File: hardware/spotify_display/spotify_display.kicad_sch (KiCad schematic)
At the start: 5 parts, among them SW1 SW_Push, SW2 SW_Push, SW3 SW_Push, U1 WEMOS_C3_mini, U2 ST7735

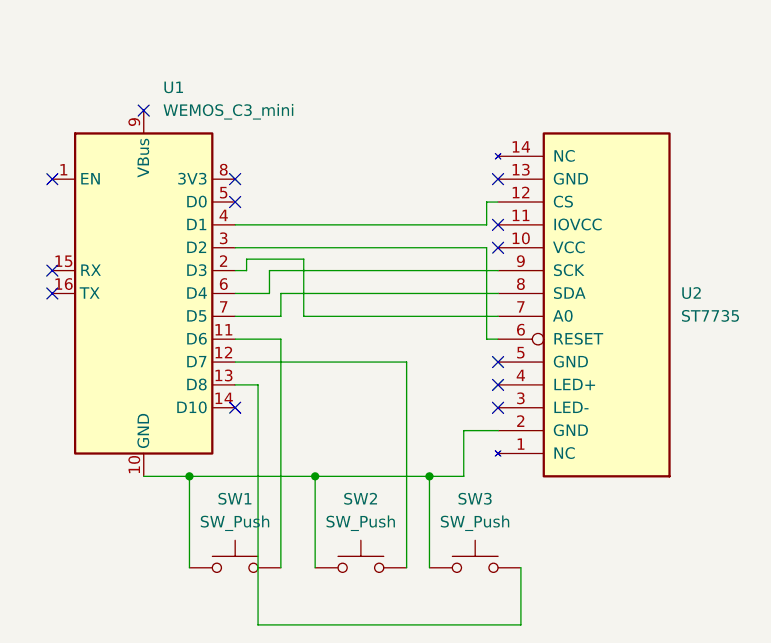
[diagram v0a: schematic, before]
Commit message: Add Rotary Encoder component and update project files
- Added a new Rotary Encoder symbol to the schematic with properties including reference, value, footprint, and description.
- Updated the KiCad project configuration to specify the plot output directory.
- Adjusted column widths in the project settings for better layout.
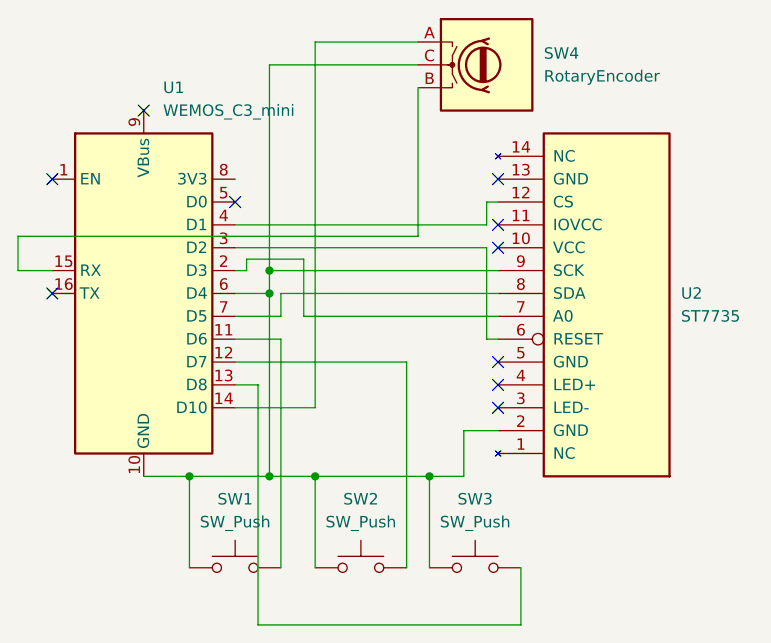
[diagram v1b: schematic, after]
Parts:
- added SW4: RotaryEncoder, Rotary_Encoder:RotaryEncoder_Alps_EC11E_Vertical_H20mm, symbol Device:RotaryEncoder
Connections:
- net at SW1.1, SW2.1, SW3.1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: now also U1.6 (D4), U2.9 (SCK), SW4.C
- net at U1.14 (D10): now also SW4.A
- net at U1.15 (RX): now also SW4.B
- no-connect marks 13 -> 10
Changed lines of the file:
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@@
 	(paper "A4")
+	(junction
+		(at 152.4 95.25)
+		(diameter 0)
+		(color 0 0 0 0)
+	)
+	(junction
+		(at 152.4 115.57)
+		(diameter 0)
+		(color 0 0 0 0)
+	)
 	(junction
 		(at 143.51 115.57)
@@
 	)
 	(junction
+		(at 152.4 92.71)
+		(diameter 0)
+		(color 0 0 0 0)
+	)
+	(junction
 		(at 170.18 115.57)
 		(diameter 0)
@@
 	)
 	(no_connect
+		(at 148.59 85.09)
+	)
+	(no_connect
 		(at 128.27 82.55)
 	)
@@
 	)
 	(no_connect
-		(at 148.59 82.55)
-	)
-	(no_connect
 		(at 128.27 95.25)
 	)
@@
 	)
 	(no_connect
-		(at 148.59 107.95)
-	)
-	(no_connect
 		(at 177.8 82.55)
 	)
@@
 		(at 177.8 90.17)
 	)
-	(no_connect
-		(at 148.59 85.09)
-	)
-	(no_connect
-		(at 128.27 92.71)
-	)
 	(wire
 		(pts
@@
 	(wire
 		(pts
+			(xy 152.4 115.57) (xy 157.48 115.57)
+		)
+		(stroke
+			(width 0)
+			(type default)
+		)
+	)
+	(wire
+		(pts
 			(xy 148.59 105.41) (xy 151.13 105.41)
 		)
@@
 	(wire
 		(pts
+			(xy 152.4 69.85) (xy 152.4 92.71)
+		)
+		(stroke
+			(width 0)
+			(type default)
+		)
+	)
+	(wire
+		(pts
 			(xy 151.13 132.08) (xy 180.34 132.08)
 		)
@@
 	(wire
 		(pts
-			(xy 143.51 115.57) (xy 157.48 115.57)
+			(xy 143.51 115.57) (xy 152.4 115.57)
 		)
 		(stroke
@@
 	(wire
 		(pts
+			(xy 168.91 69.85) (xy 152.4 69.85)
+		)
+		(stroke
+			(width 0)
+			(type default)
+		)
+	)
+	(wire
+		(pts
 			(xy 143.51 115.57) (xy 143.51 125.73)
 		)
@@
 	(wire
 		(pts
+			(xy 124.46 88.9) (xy 124.46 92.71)
+		)
+		(stroke
+			(width 0)
+			(type default)
+		)
+	)
+	(wire
+		(pts
 			(xy 156.21 97.79) (xy 177.8 97.79)
 		)
@@
 	(wire
 		(pts
-			(xy 152.4 95.25) (xy 152.4 92.71)
+			(xy 152.4 95.25) (xy 152.4 115.57)
+		)
+		(stroke
+			(width 0)
+			(type default)
+		)
+	)
+	(wire
+		(pts
+			(xy 168.91 88.9) (xy 124.46 88.9)
+		)
+		(stroke
+			(width 0)
+			(type default)
+		)
+	)
+	(wire
+		(pts
+			(xy 152.4 92.71) (xy 152.4 95.25)
+		)
+		(stroke
+			(width 0)
+			(type default)
+		)
+	)
+	(wire
+		(pts
+			(xy 124.46 92.71) (xy 128.27 92.71)
+		)
+		(stroke
+			(width 0)
+			(type default)
+		)
+	)
+	(wire
+		(pts
+			(xy 168.91 72.39) (xy 168.91 88.9)
 		)
 		(stroke
@@
 	(wire
 		(pts
+			(xy 157.48 67.31) (xy 157.48 107.95)
+		)
+		(stroke
+			(width 0)
+			(type default)
+		)
+	)
+	(wire
+		(pts
 			(xy 176.53 85.09) (xy 177.8 85.09)
 		)
@@
 	(wire
 		(pts
+			(xy 168.91 67.31) (xy 157.48 67.31)
+		)
+		(stroke
+			(width 0)
+			(type default)
+		)
+	)
+	(wire
+		(pts
 			(xy 153.67 95.25) (xy 177.8 95.25)
 		)
@@
 		(pts
 			(xy 149.86 91.44) (xy 156.21 91.44)
+		)
+		(stroke
+			(width 0)
+			(type default)
+		)
+	)
+	(wire
+		(pts
+			(xy 157.48 107.95) (xy 148.59 107.95)
 		)
 		(stroke
@@
 					(unit 1)
 				)
+			)
+		)
+	)
+	(symbol
+		(lib_id "Device:RotaryEncoder")
+		(at 176.53 69.85 0)
+		(unit 1)
+		(exclude_from_sim no)
+		(in_bom yes)
+		(on_board yes)
+		(dnp no)
+		(fields_autoplaced yes)
+		(property "Reference" "SW4"
+			(at 182.88 68.5799 0)
+			(effects
+				(font
+					(size 1.27 1.27)
+				)
+				(justify left)
+			)
+		)
+		(property "Value" "RotaryEncoder"
+			(at 182.88 71.1199 0)
+			(effects
+				(font
+					(size 1.27 1.27)
+				)
+				(justify left)
+			)
+		)
+		(property "Footprint" "Rotary_Encoder:RotaryEncoder_Alps_EC11E_Vertical_H20mm"
+			(at 172.72 65.786 0)
+			(effects
+				(font
+					(size 1.27 1.27)
+				)
+				(hide yes)
+			)
+		)
+		(property "Datasheet" "~"
+			(at 176.53 63.246 0)
+			(effects
+				(font
+					(size 1.27 1.27)
+				)
+				(hide yes)
+			)
+		)
+		(property "Description" "Rotary encoder, dual channel, incremental quadrate outputs"
+			(at 176.53 69.85 0)
+			(effects
+				(font
+					(size 1.27 1.27)
+				)
+				(hide yes)
+			)
+		)
+		(pin "C"
+		)
+		(pin "B"
+		)
+		(pin "A"
+		)
+		(instances
+			(project ""
+				(path "/4539219a-db65-428b-bdec-993c35018d0c"
+					(reference "SW4")
+					(unit 1)
+				)
